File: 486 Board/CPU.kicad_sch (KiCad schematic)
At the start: 20 parts, among them J16 Conn_02x03_Counter_Clockwise, J17 Conn_02x04_Counter_Clockwise, J18 Conn_02x03_Counter_Clockwise, U1 80486DX

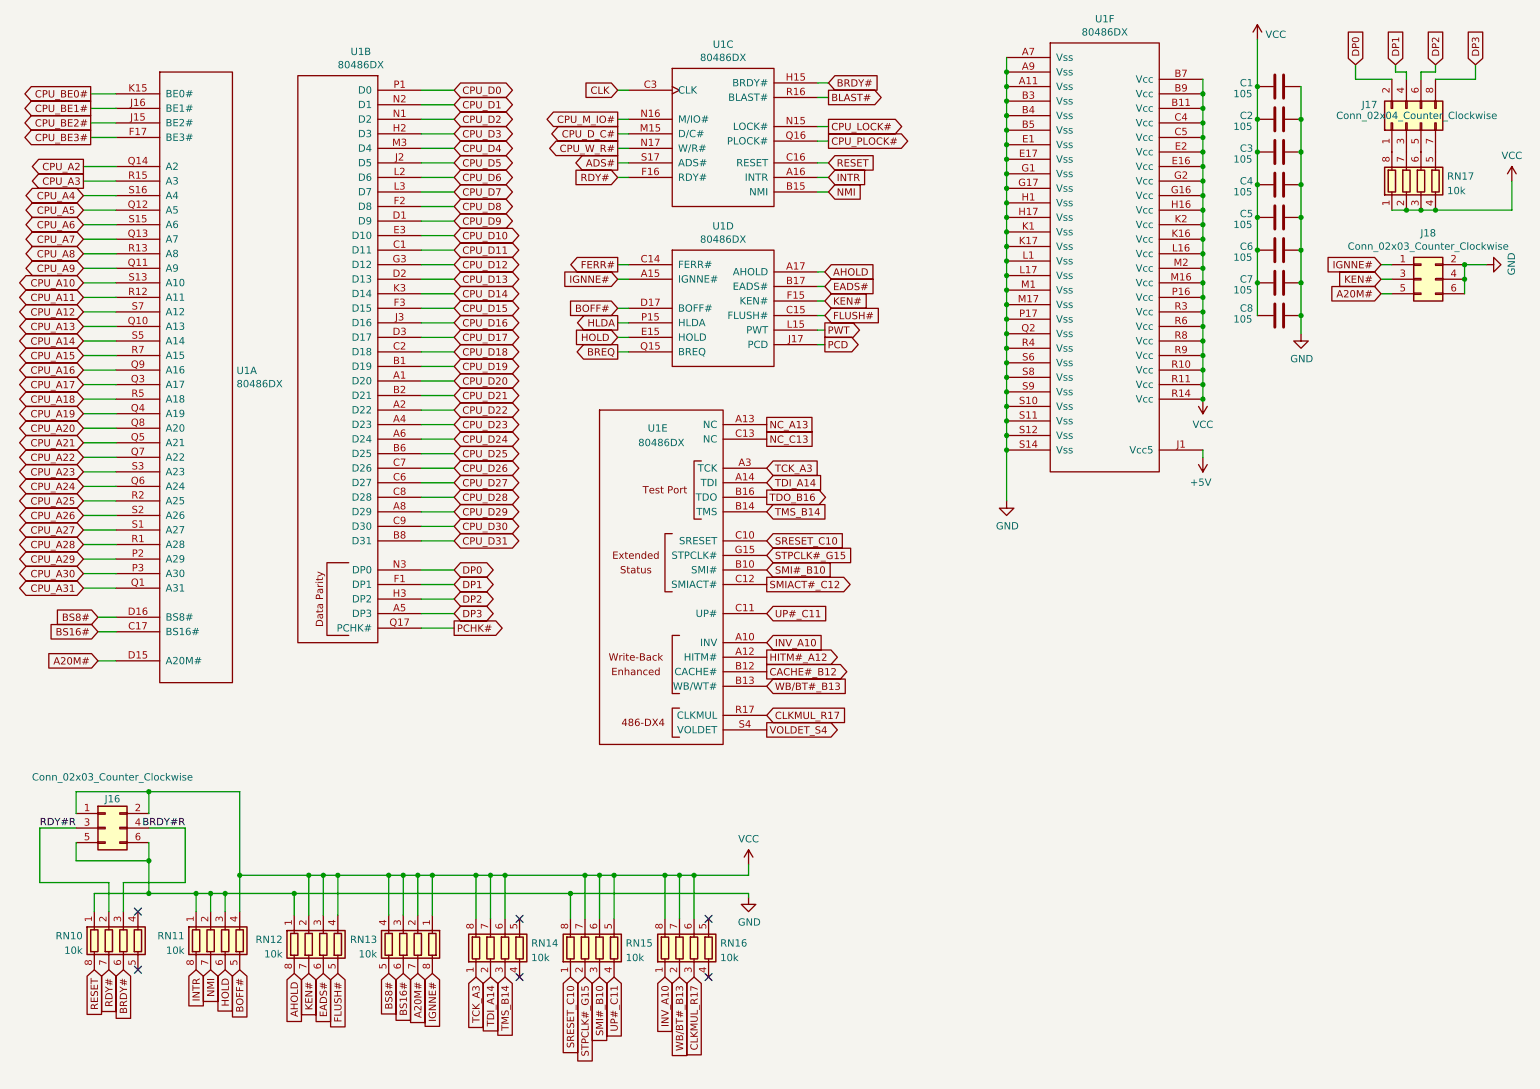
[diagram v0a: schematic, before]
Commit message: * Layout Template for eurocard format * 486 Board updated to new layout * Support board draft * Added 6u eurocard backplane meant for ATX case
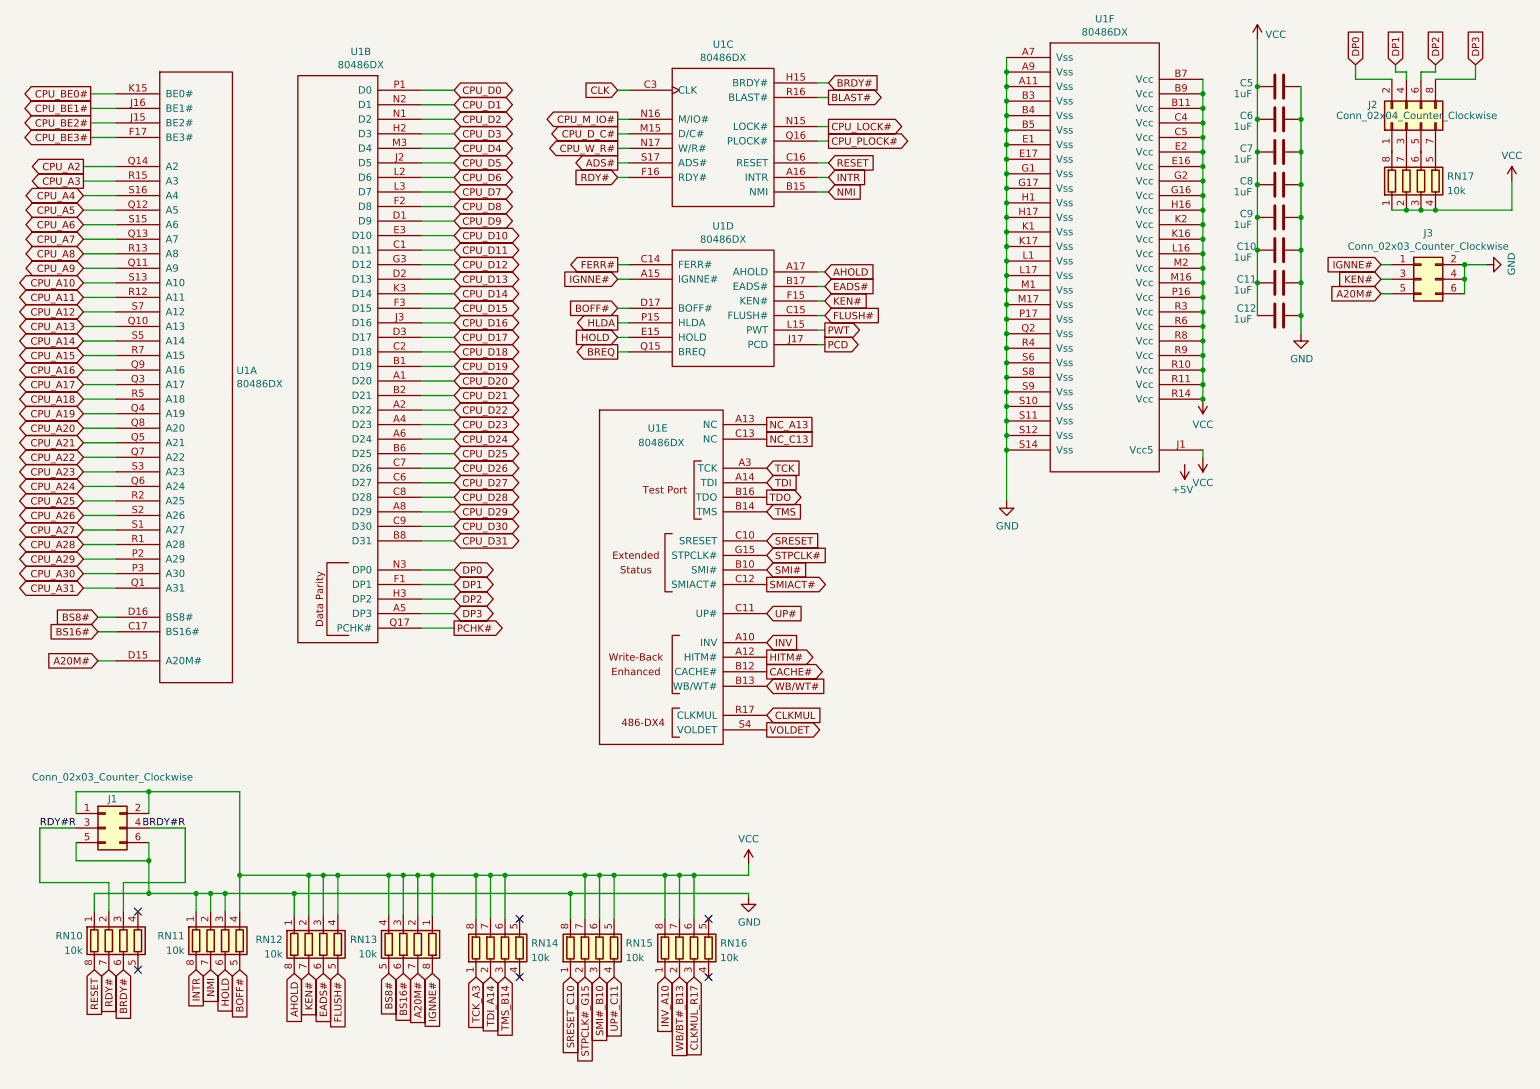
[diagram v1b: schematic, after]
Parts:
- C10: renamed from C6; value 105 -> 1uF
- C11: renamed from C7; value 105 -> 1uF
- C12: renamed from C8; value 105 -> 1uF
- C5: renamed from C1; value 105 -> 1uF
- C6: renamed from C2; value 105 -> 1uF
- C7: renamed from C3; value 105 -> 1uF
- C8: renamed from C4; value 105 -> 1uF
- C9: renamed from C5; value 105 -> 1uF
- renumbered J16 to J1, J17 to J2, J18 to J3
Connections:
- net +5V: no longer U1.J1 (Vcc5)
- net CLKMUL_R17: no longer U1.R17 (CLKMUL)
- net INV_A10: no longer U1.A10 (INV)
- net SMI#_B10: no longer U1.B10 (SMI#)
- net SRESET_C10: no longer U1.C10 (SRESET)
- net STPCLK#_G15: no longer U1.G15 (STPCLK#)
- net TCK_A3: no longer U1.A3 (TCK)
- net TDI_A14: no longer U1.A14 (TDI)
- net TMS_B14: no longer U1.B14 (TMS)
- net UP#_C11: no longer U1.C11 (UP#)
- net VCC: now also U1.J1 (Vcc5)
- net WB/BT#_B13: no longer U1.B13 (WB/WT#)
- net CACHE#_B12 renamed CACHE#
- net HITM#_A12 renamed HITM#
- net SMIACT#_C12 renamed SMIACT#
- net TDO_B16 renamed TDO
- net VOLDET_S4 renamed VOLDET
- new net CLKMUL: U1.R17 (CLKMUL)
- new net INV: U1.A10 (INV)
- new net SMI#: U1.B10 (SMI#)
- new net SRESET: U1.C10 (SRESET)
- new net STPCLK#: U1.G15 (STPCLK#)
- new net TCK: U1.A3 (TCK)
- new net TDI: U1.A14 (TDI)
- new net TMS: U1.B14 (TMS)
- new net UP#: U1.C11 (UP#)
- new net WB/WT#: U1.B13 (WB/WT#)
